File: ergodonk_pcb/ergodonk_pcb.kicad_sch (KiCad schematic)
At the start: 114 parts, among them J1 AudioJack4, Q1 TIP120

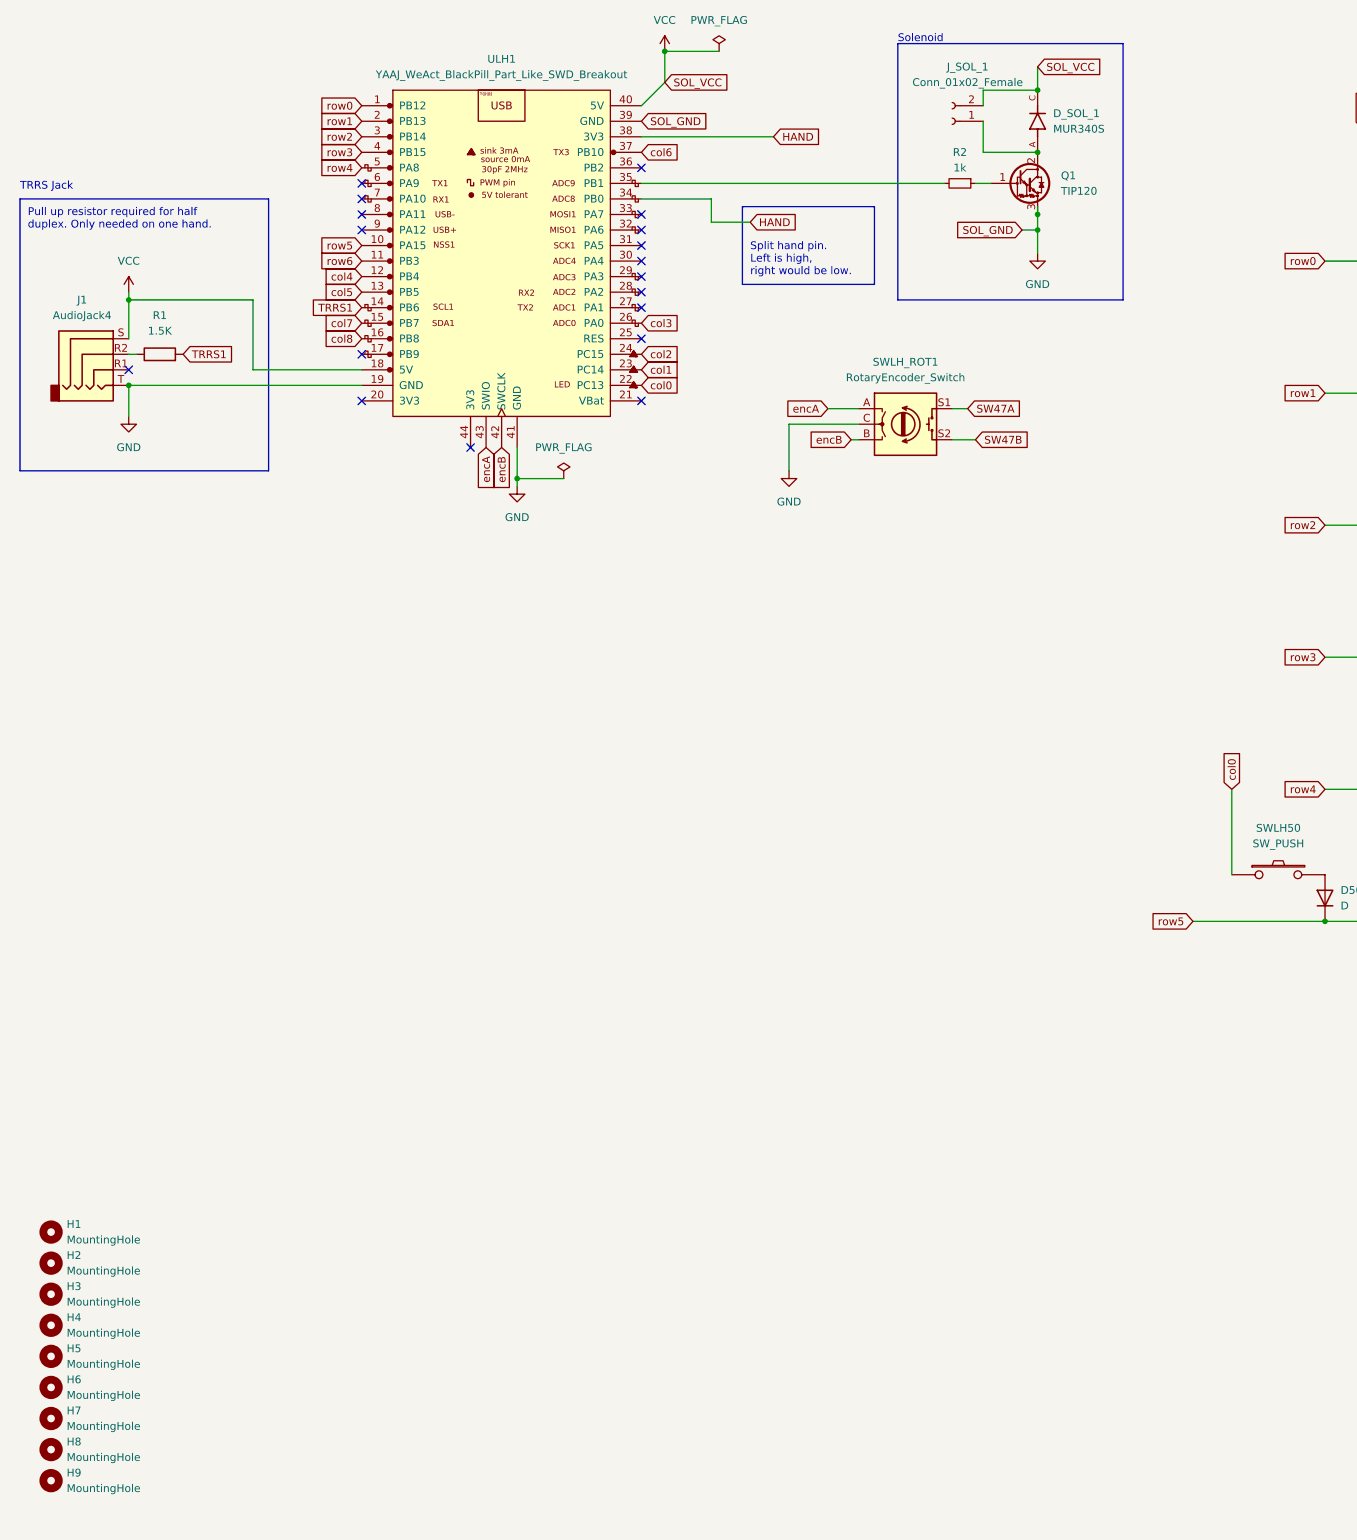
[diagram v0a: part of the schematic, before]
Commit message: LH single side pcb first draft complete sent this version to jlcpcb for prototype production
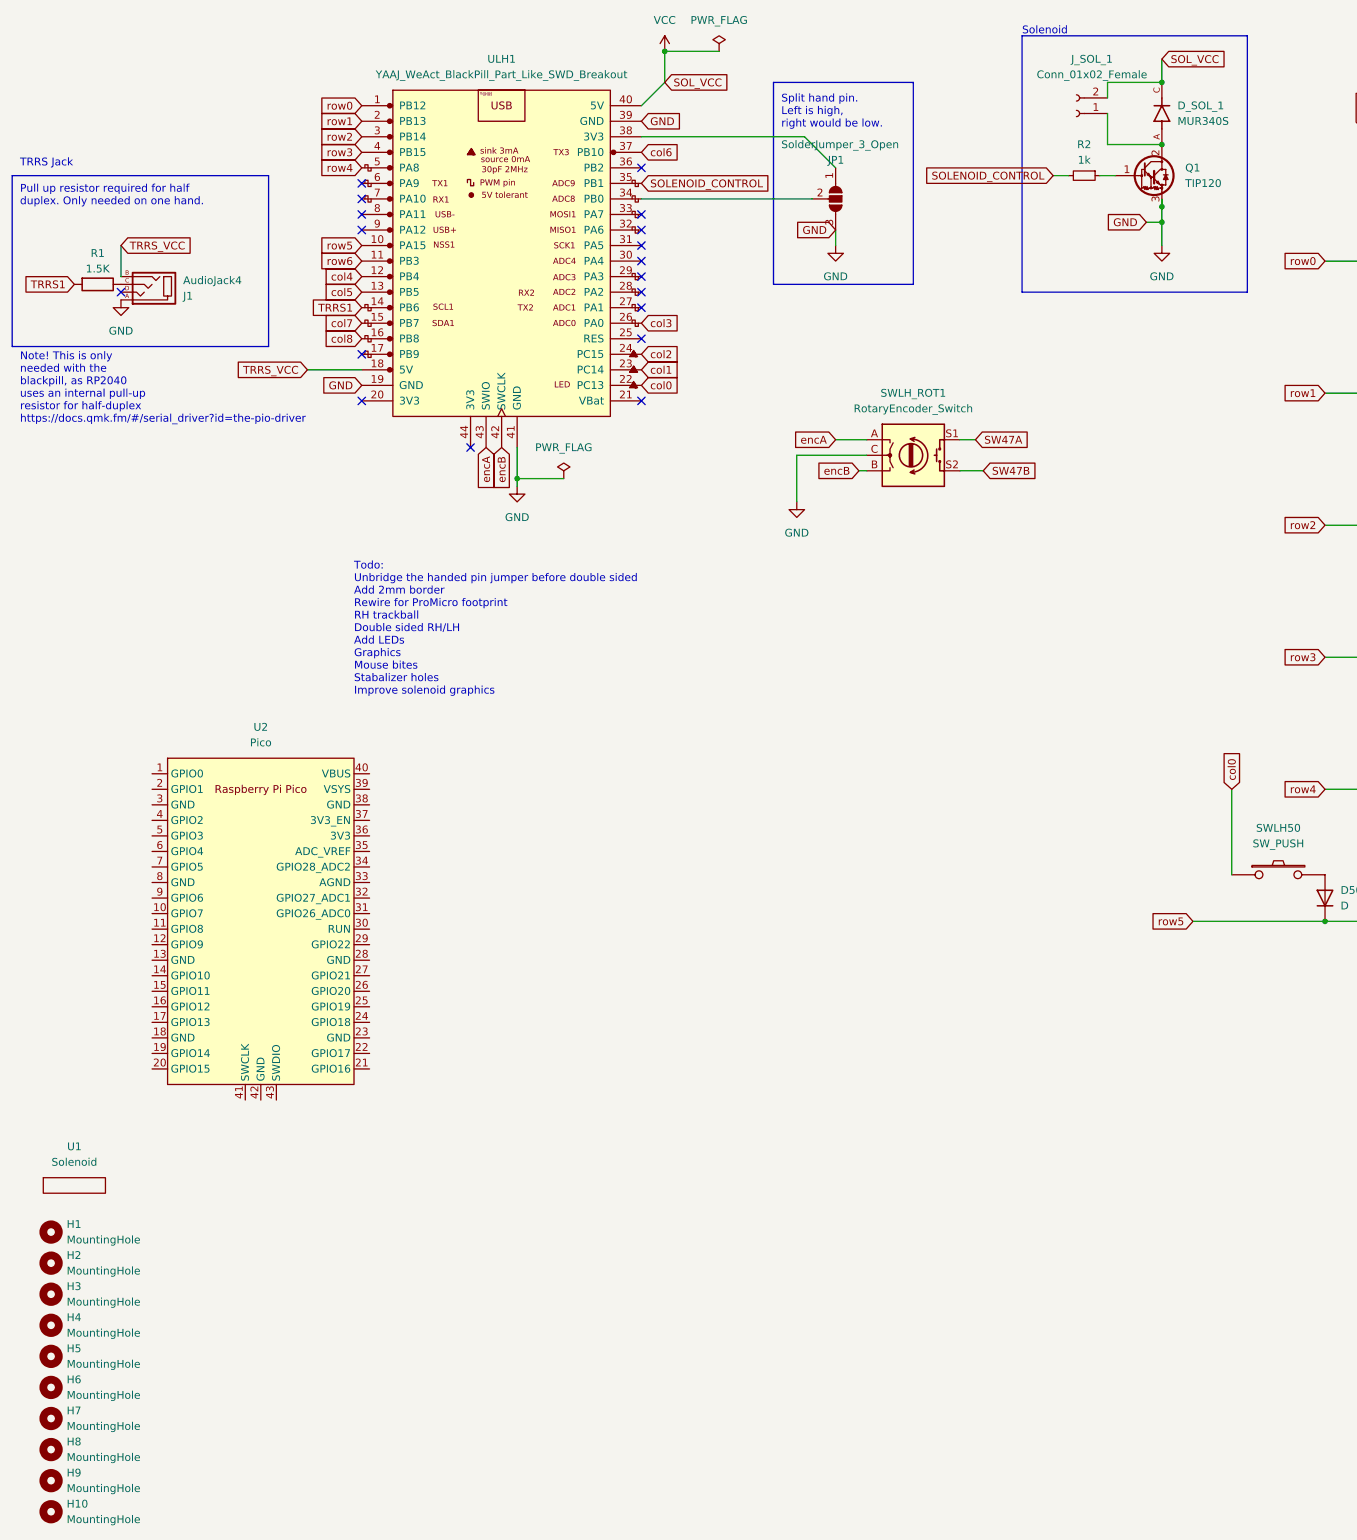
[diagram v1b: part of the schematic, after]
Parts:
- added H10: MountingHole, MountingHole:MountingHole_2.2mm_M2_Pad_Via, symbol Mechanical:MountingHole
- added JP1: SolderJumper_3_Open, Keebio-Parts:SolderJumper, symbol Jumper:SolderJumper_3_Open
- added U1: Solenoid, ergodonk_kicad_library:uxcell a14092600ux0438 solenoid, symbol Neff_KiCad_Symbol_library:Solenoid
- added U2: Pico, MCU_RaspberryPi_and_Boards:RPi_Pico_SMD_TH, symbol MCU_RaspberryPi_and_Boards:Pico
- H1, H2, H3, H4, H5, H6, H7, H8, H9: footprint MountingHole:MountingHole_3.2mm_M3_Pad_Via -> MountingHole:MountingHole_2.2mm_M2_Pad_Via
- J1: footprint kbd:MJ-4PP-9_1side -> kbd:MJ-4PP-9; symbol Connector:AudioJack4 -> kbd:MJ-4PP-9
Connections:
- net GND: now also J1.A, JP1.3 (B); no longer J1.T
- net VCC: no longer J1.S, ULH1.18 (5V)
- net SOLENOID_CONTROL: now reaches R2.2, ULH1.35 (PB1)
- net at R1.1: now also J1.C; no longer J1.R2
- net HAND: no longer names the net of ULH1.38 (3V3)
- net HAND: now also JP1.1 (A); no longer ULH1.34 (PB0)
- new net: JP1.2 (C), ULH1.34 (PB0)
- new net TRRS_VCC: J1.B, ULH1.18 (5V)
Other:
- note added: "Note! This is only needed with the blackpill, as RP2040 uses an internal pull-up resistor for half-duplex https://docs.qmk.fm/#/serial_driver?id=the-pio-driver"
- note added: "Todo: Unbridge the handed pin jumper before double sided Add 2mm border Rewire for ProMicro footprint RH trackball Double sided RH/LH Add LEDs Graphics Mouse bites Stabalizer holes Improve solenoid graphics"
- moved on the sheet: D_SOL_1, J_SOL_1, Q1, R2, SWLH_ROT1

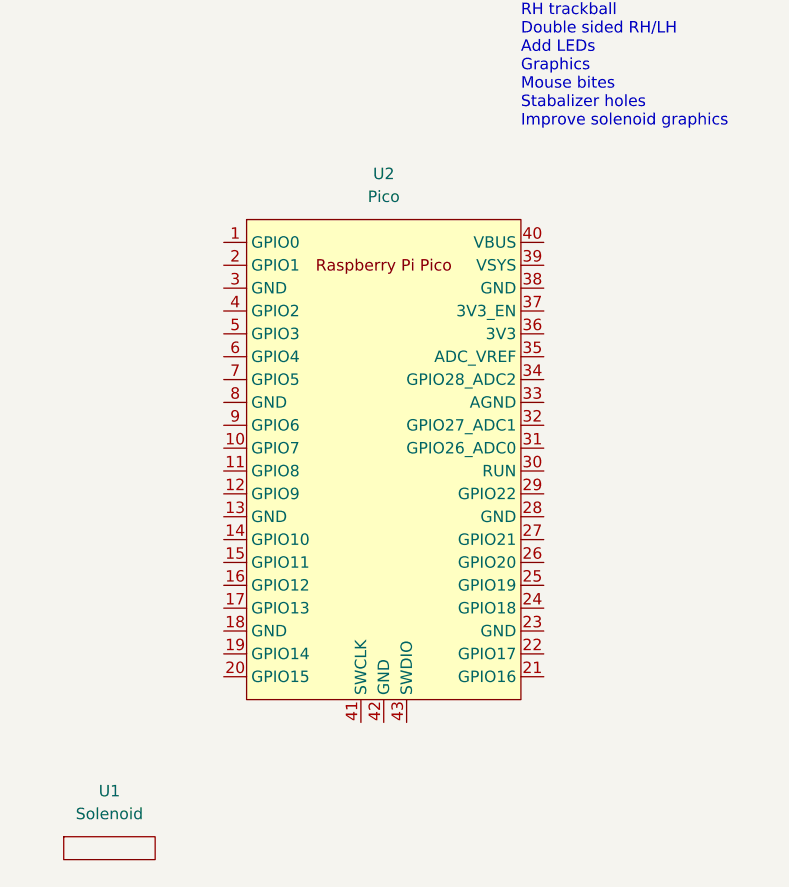
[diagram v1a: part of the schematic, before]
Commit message: Synchronized updated footprints with schematics
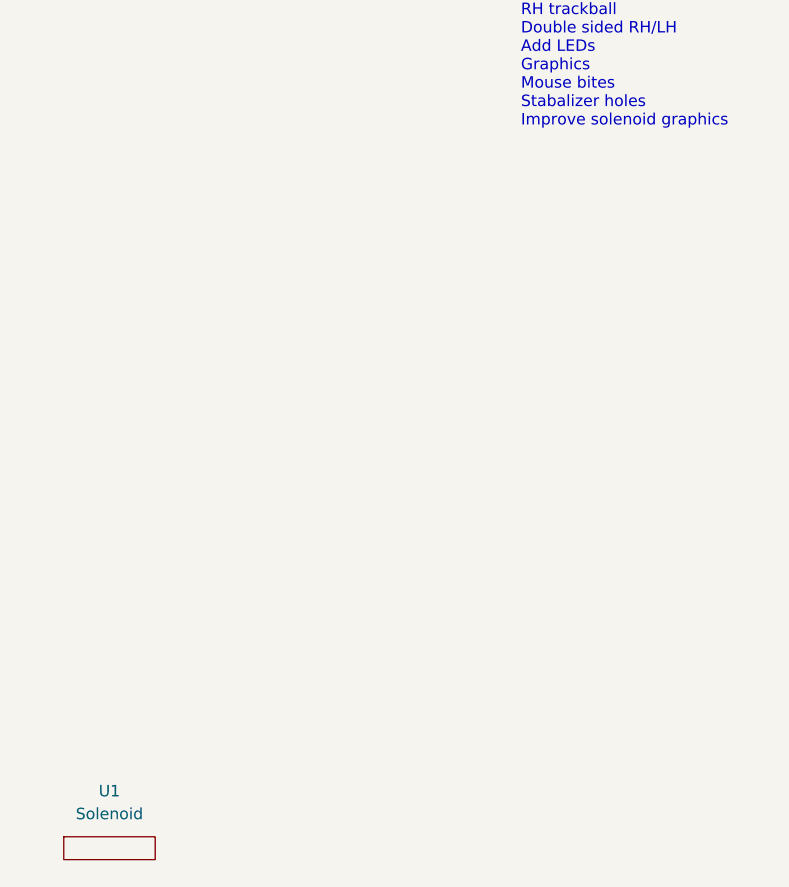
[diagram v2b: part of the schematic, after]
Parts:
- removed U2: Pico, MCU_RaspberryPi_and_Boards:RPi_Pico_SMD_TH, symbol MCU_RaspberryPi_and_Boards:Pico
- D_SOL_1: footprint MUR340S:DIOM6859X262N -> Neffs_kicad_footprint_library:MUR340S_IN4004_TH
- SWLH_ROT1: footprint Keebio-Parts:RotaryEncoder_EC11 -> ergodonk_kicad_library:RotaryEncoder_EC11_with_MX_hotswap_v2
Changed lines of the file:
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@@
     (property "Reference" "SWLH_ROT1" (id 0) (at 161.29 74.93 0))
     (property "Value" "RotaryEncoder_Switch" (id 1) (at 161.29 77.47 0))
-    (property "Footprint" "Keebio-Parts:RotaryEncoder_EC11" (id 2) (at 157.48 81.026 0)
+    (property "Footprint" "ergodonk_kicad_library:RotaryEncoder_EC11_with_MX_hotswap_v2" (id 2) (at 157.48 81.026 0)
       (effects (font (size 1.27 1.27)) hide)
     )
@@
     (pin "1")
   )
-  (symbol (lib_id "MCU_RaspberryPi_and_Boards:Pico") (at 54.61 161.29 0) (unit 1)
-    (in_bom yes) (on_board yes) (fields_autoplaced)
-    (property "Reference" "U2" (id 0) (at 54.61 129.54 0))
-    (property "Value" "Pico" (id 1) (at 54.61 132.08 0))
-    (property "Footprint" "MCU_RaspberryPi_and_Boards:RPi_Pico_SMD_TH" (id 2) (at 54.61 161.29 90)
-      (effects (font (size 1.27 1.27)) hide)
-    )
-    (property "Datasheet" "" (id 3) (at 54.61 161.29 0)
-      (effects (font (size 1.27 1.27)) hide)
-    )
-    (pin "1")
-    (pin "10")
-    (pin "11")
-    (pin "12")
-    (pin "13")
-    (pin "14")
-    (pin "15")
-    (pin "16")
-    (pin "17")
-    (pin "18")
-    (pin "19")
-    (pin "2")
-    (pin "20")
-    (pin "21")
-    (pin "22")
-    (pin "23")
-    (pin "24")
-    (pin "25")
-    (pin "26")
-    (pin "27")
-    (pin "28")
-    (pin "29")
-    (pin "3")
-    (pin "30")
-    (pin "31")
-    (pin "32")
-    (pin "33")
-    (pin "34")
-    (pin "35")
-    (pin "36")
-    (pin "37")
-    (pin "38")
-    (pin "39")
-    (pin "4")
-    (pin "40")
-    (pin "41")
-    (pin "42")
-    (pin "43")
-    (pin "5")
-    (pin "6")
-    (pin "7")
-    (pin "8")
-    (pin "9")
-  )
   (symbol (lib_id "Device:D") (at 293.37 114.3 90) (unit 1)
     (in_bom yes) (on_board yes) (fields_autoplaced)
@@
       (effects (font (size 1.27 1.27)) (justify right))
     )
-    (property "Footprint" "MUR340S:DIOM6859X262N" (id 2) (at 201.93 29.21 0)
+    (property "Footprint" "Neffs_kicad_footprint_library:MUR340S_IN4004_TH" (id 2) (at 201.93 29.21 0)
       (effects (font (size 1.27 1.27)) (justify bottom) hide)
     )
@@
     )
     (path "/43a0c72e-039e-4a12-b9f3-7a0bb9910ee2"
-      (reference "D_SOL_1") (unit 1) (value "MUR340S") (footprint "MUR340S:DIOM6859X262N")
+      (reference "D_SOL_1") (unit 1) (value "MUR340S") (footprint "Neffs_kicad_footprint_library:MUR340S_IN4004_TH")
     )
     (path "/1ff9d668-1af7-49f1-99e0-ea0235d3888d"
@@
     )
     (path "/1094122a-69fb-42ce-a934-8cba93263bdc"
-      (reference "SWLH_ROT1") (unit 1) (value "RotaryEncoder_Switch") (footprint "Keebio-Parts:RotaryEncoder_EC11")
+      (reference "SWLH_ROT1") (unit 1) (value "RotaryEncoder_Switch") (footprint "ergodonk_kicad_library:RotaryEncoder_EC11_with_MX_hotswap_v2")
     )
     (path "/a911a847-2802-4dd4-b6d0-33573b4d1ba3"
       (reference "U1") (unit 1) (value "Solenoid") (footprint "ergodonk_kicad_library:uxcell a14092600ux0438 solenoid")
     )
-    (path "/16993a0a-a312-451e-aa9f-867977fb2b58"
-      (reference "U2") (unit 1) (value "Pico") (footprint "MCU_RaspberryPi_and_Boards:RPi_Pico_SMD_TH")
-    )
     (path "/c103fff7-a3eb-4bac-9615-edfd2f702179"

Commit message: Moved customezed footprints to seperate library and updated schematic association
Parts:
- SWLH1, SWLH11, SWLH12, SWLH13, SWLH14, SWLH15, SWLH16, SWLH17, SWLH18, SWLH2, SWLH22, SWLH23, SWLH24, SWLH25, SWLH26, SWLH27, SWLH28, SWLH3, SWLH32, SWLH33, SWLH34, SWLH35, SWLH36, SWLH37, SWLH38, SWLH4, SWLH42, SWLH43, SWLH44, SWLH45, SWLH46, SWLH48, SWLH5, SWLH52, SWLH53, SWLH54, SWLH58, SWLH6, SWLH68, SWLH7: footprint kbd:CherryMX_Hotswap -> ergodonk_kicad_library:CherryMX_Hotswap
- SWLH21: footprint kbd:CherryMX_Hotswap_1.5u -> ergodonk_kicad_library:CherryMX_Hotswap_1.5u
- SWLH31: footprint kbd:CherryMX_Hotswap_1.75u_ergodonk -> ergodonk_kicad_library:CherryMX_Hotswap_1.75u_ergodonk
- SWLH41, SWLH56, SWLH57: footprint kbd:CherryMX_Hotswap_2u_ergodonk -> ergodonk_kicad_library:CherryMX_Hotswap_2u_ergodonk
- SWLH50, SWLH51: footprint kbd:CherryMX_Hotswap_1.25u_ergodonk -> ergodonk_kicad_library:CherryMX_Hotswap_1.25u_ergodonk
- SWLH65: footprint kbd:CherryMX_Hotswap_1.25u_Vert_ergodonk -> ergodonk_kicad_library:CherryMX_Hotswap_1.25u_Vert_ergodonk

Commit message: Added 2u Screw in stabalizers and rerouted wiring
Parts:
- SWLH41, SWLH56, SWLH57: footprint ergodonk_kicad_library:CherryMX_Hotswap_2u_ergodonk -> ergodonk_kicad_library:CherryMX_Hotswap_2u_ergodonk_Stabs
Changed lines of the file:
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@@
     (property "Reference" "SWLH56" (id 0) (at 350.52 146.05 0))
     (property "Value" "SW_PUSH" (id 1) (at 350.52 148.59 0))
-    (property "Footprint" "ergodonk_kicad_library:CherryMX_Hotswap_2u_ergodonk" (id 2) (at 350.52 153.67 0)
+    (property "Footprint" "ergodonk_kicad_library:CherryMX_Hotswap_2u_ergodonk_Stabs" (id 2) (at 350.52 153.67 0)
       (effects (font (size 1.27 1.27)) hide)
     )
@@
     (property "Reference" "SWLH57" (id 0) (at 372.11 146.05 0))
     (property "Value" "SW_PUSH" (id 1) (at 372.11 148.59 0))
-    (property "Footprint" "ergodonk_kicad_library:CherryMX_Hotswap_2u_ergodonk" (id 2) (at 372.11 153.67 0)
+    (property "Footprint" "ergodonk_kicad_library:CherryMX_Hotswap_2u_ergodonk_Stabs" (id 2) (at 372.11 153.67 0)
       (effects (font (size 1.27 1.27)) hide)
     )
@@
     (property "Reference" "SWLH41" (id 0) (at 242.57 124.46 0))
     (property "Value" "SW_PUSH" (id 1) (at 242.57 127 0))
-    (property "Footprint" "ergodonk_kicad_library:CherryMX_Hotswap_2u_ergodonk" (id 2) (at 242.57 132.08 0)
+    (property "Footprint" "ergodonk_kicad_library:CherryMX_Hotswap_2u_ergodonk_Stabs" (id 2) (at 242.57 132.08 0)
       (effects (font (size 1.27 1.27)) hide)
     )
@@
     )
     (path "/a46a17f8-62ac-492f-b055-fc52c75dae86"
-      (reference "SWLH41") (unit 1) (value "SW_PUSH") (footprint "ergodonk_kicad_library:CherryMX_Hotswap_2u_ergodonk")
+      (reference "SWLH41") (unit 1) (value "SW_PUSH") (footprint "ergodonk_kicad_library:CherryMX_Hotswap_2u_ergodonk_Stabs")
     )
     (path "/c15dac7b-0e67-4348-b1cc-38f890301c39"
@@
     )
     (path "/2b4de526-ee32-49c4-ba40-3a3a92ad67bc"
-      (reference "SWLH56") (unit 1) (value "SW_PUSH") (footprint "ergodonk_kicad_library:CherryMX_Hotswap_2u_ergodonk")
+      (reference "SWLH56") (unit 1) (value "SW_PUSH") (footprint "ergodonk_kicad_library:CherryMX_Hotswap_2u_ergodonk_Stabs")
     )
     (path "/5b43806e-8d2f-432c-a63b-c66018a18e93"
-      (reference "SWLH57") (unit 1) (value "SW_PUSH") (footprint "ergodonk_kicad_library:CherryMX_Hotswap_2u_ergodonk")
+      (reference "SWLH57") (unit 1) (value "SW_PUSH") (footprint "ergodonk_kicad_library:CherryMX_Hotswap_2u_ergodonk_Stabs")
     )
     (path "/28f93af9-5b22-42b8-823f-43d101fe16ea"

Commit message: Updated schematic to V2 wiring - frees up one more pin[B (b3)
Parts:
- renumbered D28 to D18, D38 to D28, D48 to D38, D58 to D48, D65 to D55, D68 to D58, D18 to D8, SWLH28 to SWLH18, SWLH38 to SWLH28, SWLH48 to SWLH38, SWLH58 to SWLH48, SWLH65 to SWLH55, SWLH68 to SWLH58, SWLH18 to SWLH8
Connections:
- net row5 is gone; now on net row4: D48.1 (K), D50.1 (K), D51.1 (K), D52.1 (K), D53.1 (K), D54.1 (K), D56.1 (K), D57.1 (K), ULH1.10 (PA15)
- net row0: now also D7.2 (A), D8.1 (K), SWLH7.2
- net row1: now also D18.1 (K); no longer D8.1 (K)
- net row2: now also D28.1 (K); no longer D18.1 (K)
- net row3: now also D38.1 (K); no longer D28.1 (K)
- net row4: now also D54.2 (A), D55.1 (K), D56.2 (A), D58.1 (K), SWLH54.2, SWLH56.2; no longer D38.1 (K)
- removed net row6: D55.1 (K), D58.1 (K), ULH1.11 (PB3)
- no-connect marks 18 -> 20
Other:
- note added: "This is the V2 wiring - Firmware has not been updated to match yet."
- moved on the sheet: D18, D28, D38, D48, D55, D58, D8, SWLH18, SWLH28, SWLH38, SWLH48, SWLH55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
